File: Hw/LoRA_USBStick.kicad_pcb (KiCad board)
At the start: 2 copper layers, 61.5 x 18.7 mm, 18 parts, among them J10 USB_B, J4 SWD, SW1 RST, U1 ATSAMD21E, U2 RFM95W-868S2, U3 AP2112K-3.3

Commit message: add usb c and R
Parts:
- removed J10: USB_B, Connectors:C46394
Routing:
- net /D+: track 28.3 -> 22.9 mm
- net VBUS: track 10.6 -> 5.77 mm
- net /D-: track 30.8 -> 27.2 mm
- net GND: track 60.6 -> 58.9 mm, vias 26 -> 25

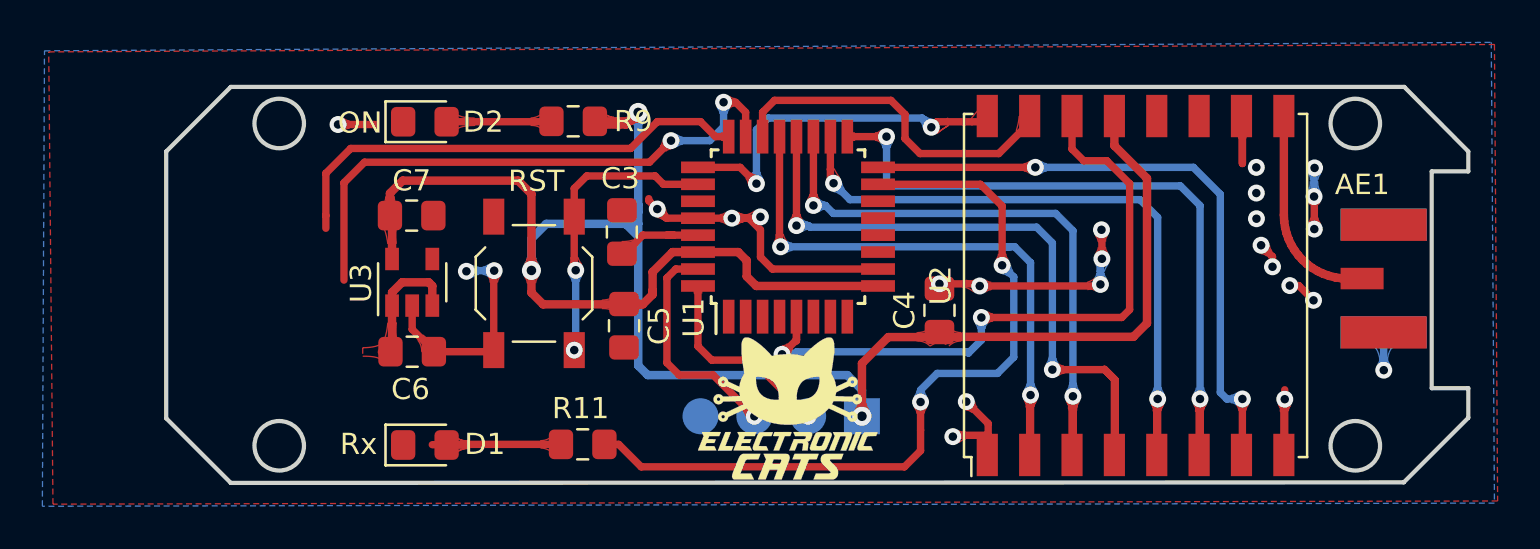
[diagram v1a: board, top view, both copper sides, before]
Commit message: Change_usb-C
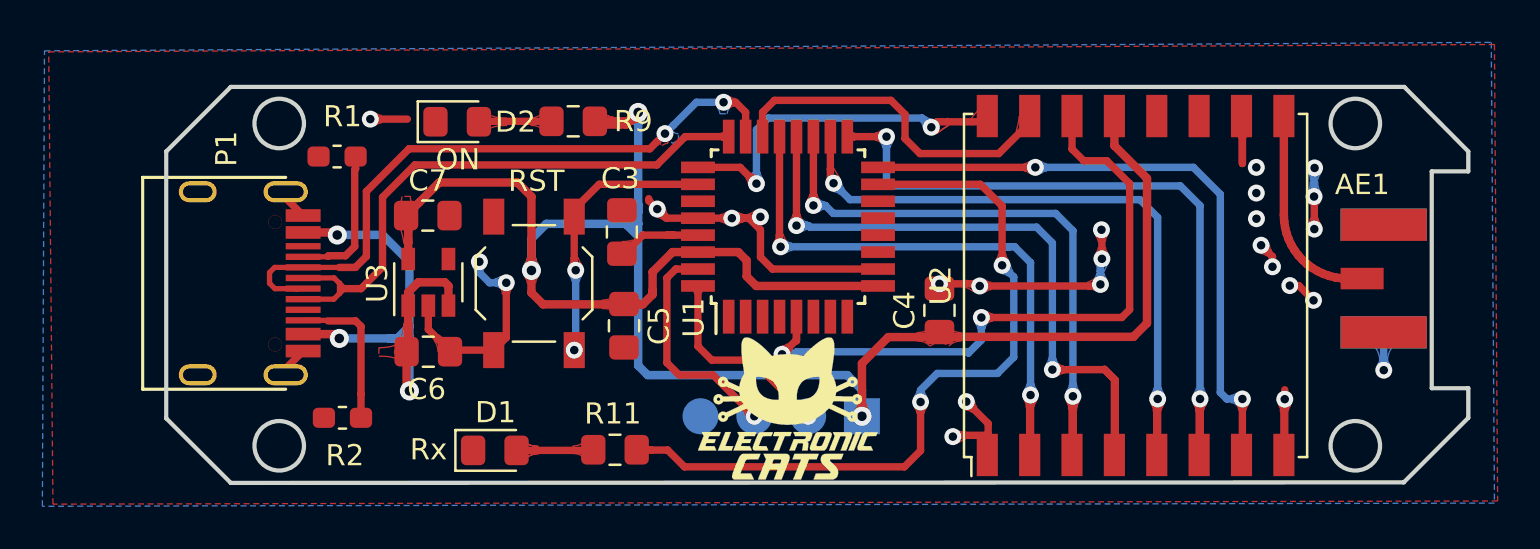
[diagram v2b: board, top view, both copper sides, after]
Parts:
- added P1: USB_C_Plug_USB2.0, Connectors:C393939, F.Cu at (122.4, 114.0)
- added R1: 5K1, Resistor_SMD:R_0603_1608Metric_Pad1.05x0.95mm_HandSolder, F.Cu at (124.9, 108.1)
- added R2: 5K1, Resistor_SMD:R_0603_1608Metric_Pad1.05x0.95mm_HandSolder, F.Cu at (125.1, 120.4)
- moved D1 3.31 mm to (132.3, 121.9)
- moved R11 1.55 mm to (138.0, 121.9)
- moved D2 1.52 mm to (130.5, 106.4)
- moved C6 0.76 mm to (129.2, 117.3)
- moved C7 0.76 mm to (129.1, 110.8)
- moved U3 0.76 mm to (129.2, 114.0)
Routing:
- net VBUS: track 5.77 -> 26.4 mm, vias 0 -> 3
- net Net-(P1-PadB5): track 0.00 -> 7.17 mm
- net Net-(P1-PadA5): track 0.00 -> 6.90 mm
- net /D+: track 22.9 -> 27.9 mm
- net Net-(D1-Pad2): track 8.09 -> 3.68 mm
- net /D-: track 27.2 -> 31.2 mm
- net GND: track 58.9 -> 62.0 mm
- net /Rx_LED: track 37.2 -> 35.6 mm
- net +3V3: track 98.9 -> 97.3 mm
- net Net-(D2-Pad2): track 4.60 -> 3.46 mm
- net /RST: track 13.9 -> 13.0 mm
- added copper zone on F.Cu, net /D-
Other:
- net class Default: trace_width 0.35 -> 0.25

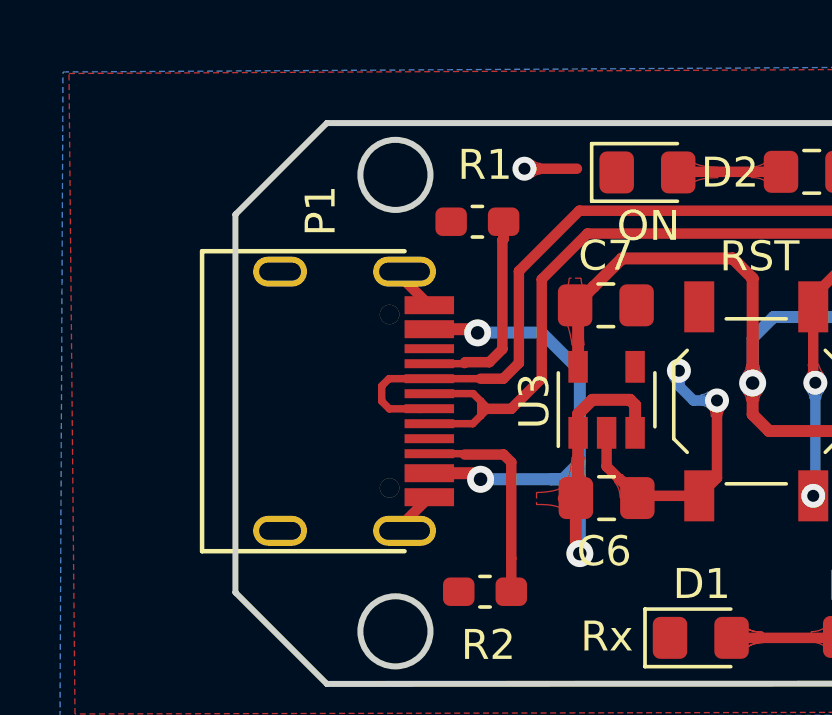
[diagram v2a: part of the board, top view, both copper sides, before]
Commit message: Change_in_connector
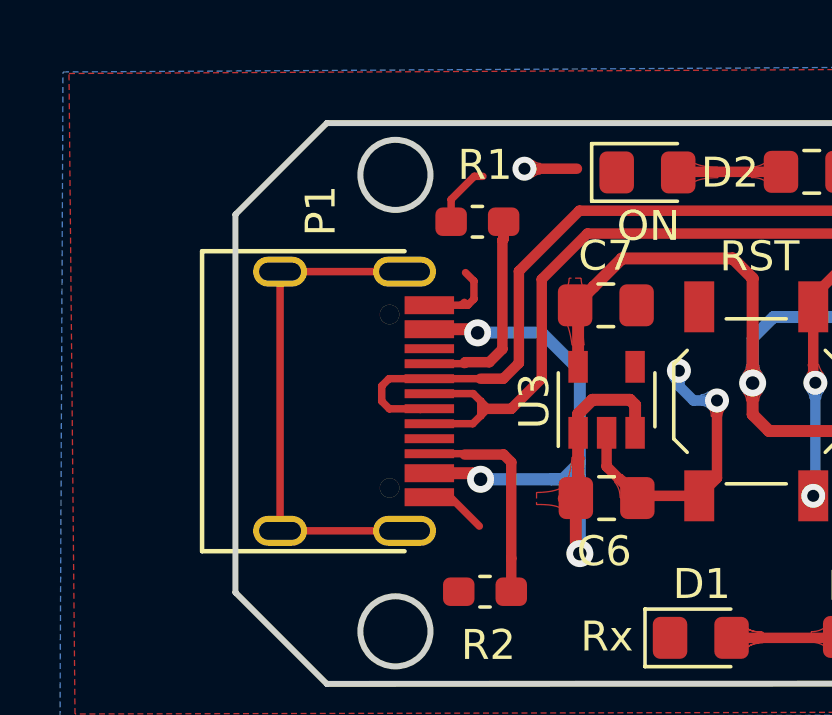
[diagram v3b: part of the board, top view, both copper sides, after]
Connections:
- P1 pad S1: GND -> Net-(P1-PadS1)
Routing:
- net Net-(P1-PadS1): track 0.00 -> 17.3 mm
- net GND: track 62.0 -> 66.0 mm
